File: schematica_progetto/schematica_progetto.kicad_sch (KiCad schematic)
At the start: 7 parts

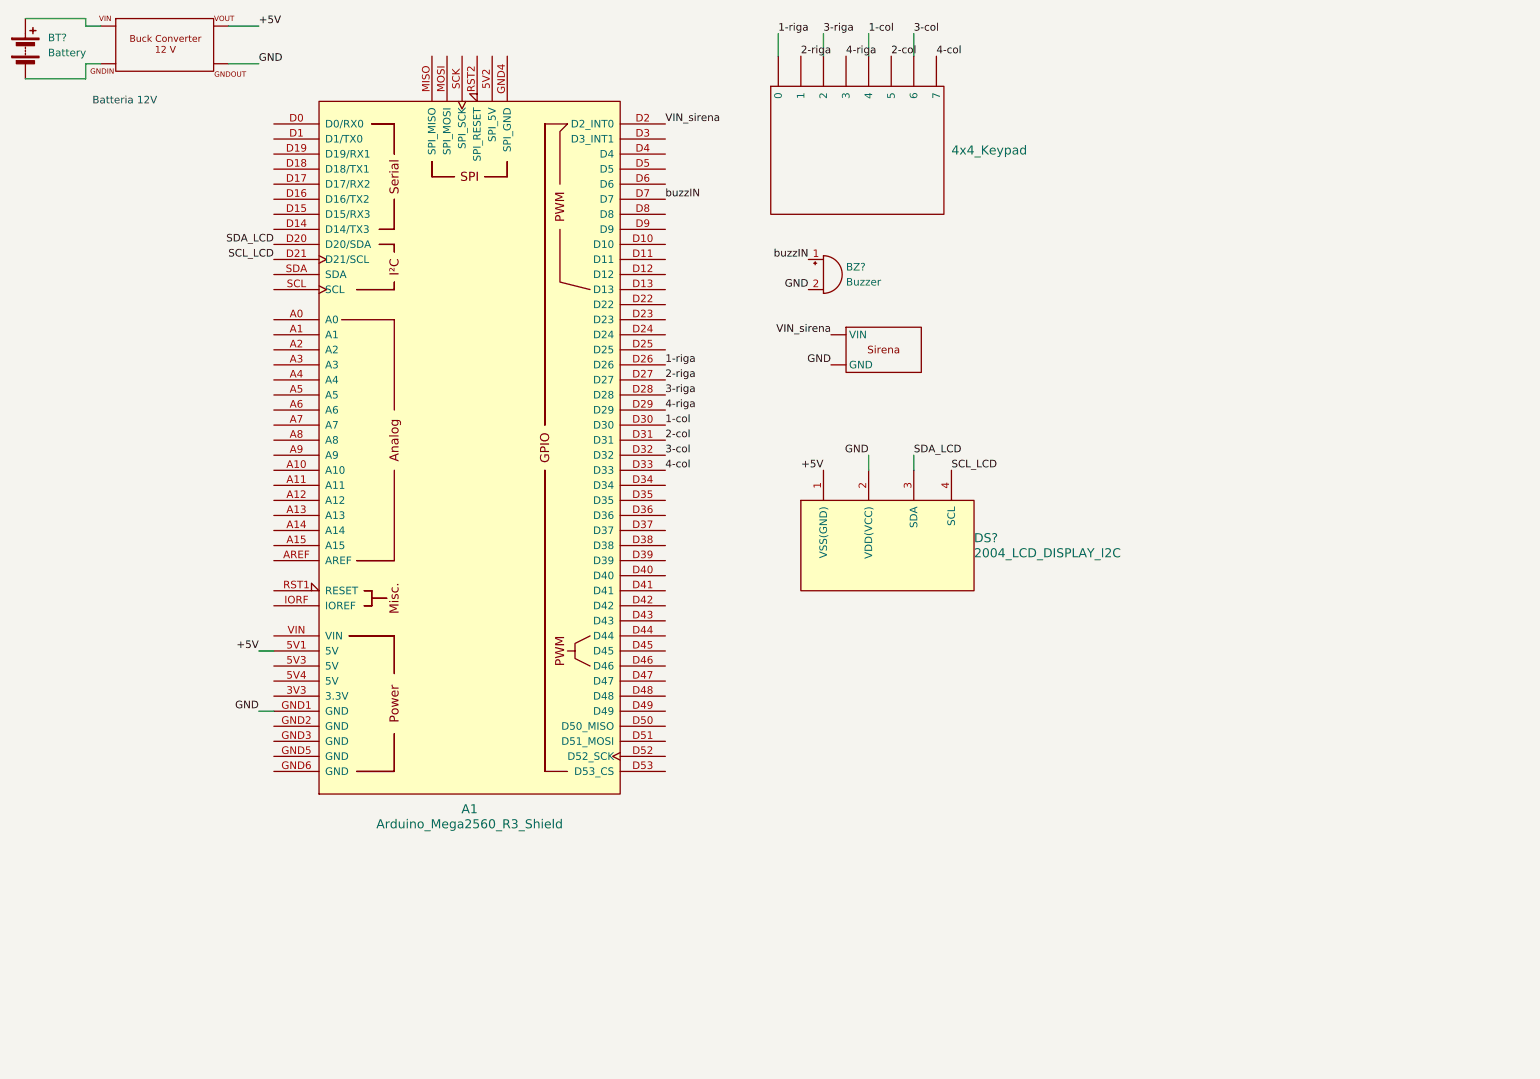
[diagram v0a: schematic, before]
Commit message: Inserito nella schematica sistema di controllo dei LED dei pulsanti. Terminata la schematica
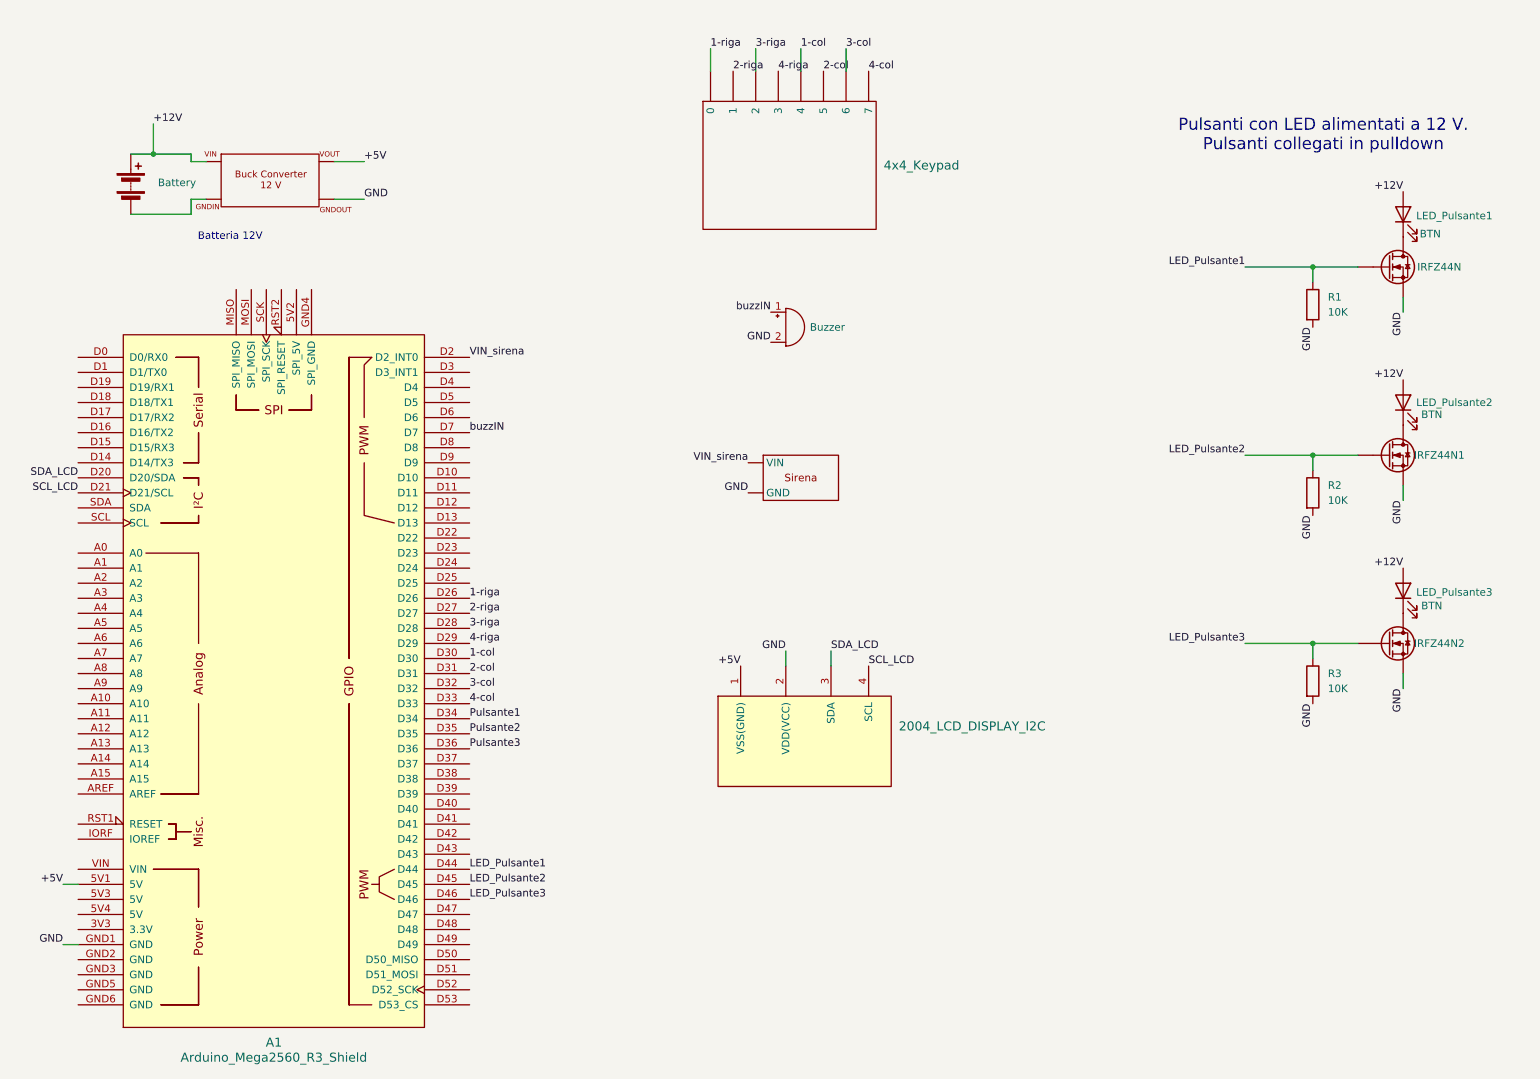
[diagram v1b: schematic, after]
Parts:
- added IRFZ44N, IRFZ44N1, IRFZ44N2: (no value), symbol Device:Q_NMOS
- added LED_Pulsante1, LED_Pulsante2, LED_Pulsante3: BTN, symbol Device:LED
- added R1, R2, R3: 10K, symbol Device:R
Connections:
- net GND: now also IRFZ44N.S, IRFZ44N1.S, IRFZ44N2.S, R1.2, R2.2, R3.2
- net +12V: now reaches BT?.1 (+), U?.
- net +12V: now also LED_Pulsante1.2 (A), LED_Pulsante2.2 (A), LED_Pulsante3.2 (A)
- net Pulsante1: now reaches A1.D34
- net Pulsante2: now reaches A1.D35
- net Pulsante3: now reaches A1.D36
- net LED_Pulsante1: now reaches A1.D44
- net LED_Pulsante1: now also IRFZ44N.G, R1.1
- net LED_Pulsante2: now reaches A1.D45
- net LED_Pulsante2: now also IRFZ44N1.G, R2.1
- net LED_Pulsante3: now reaches A1.D46
- net LED_Pulsante3: now also IRFZ44N2.G, R3.1
- new net: IRFZ44N1.D, LED_Pulsante2.1 (K)
- new net: IRFZ44N2.D, LED_Pulsante3.1 (K)
- new net: IRFZ44N.D, LED_Pulsante1.1 (K)
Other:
- note added: "Pulsanti con LED alimentati a 12 V. Pulsanti collegati in pulldown"
- moved on the sheet: A1

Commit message: Aggiunto sirena e accellerometro
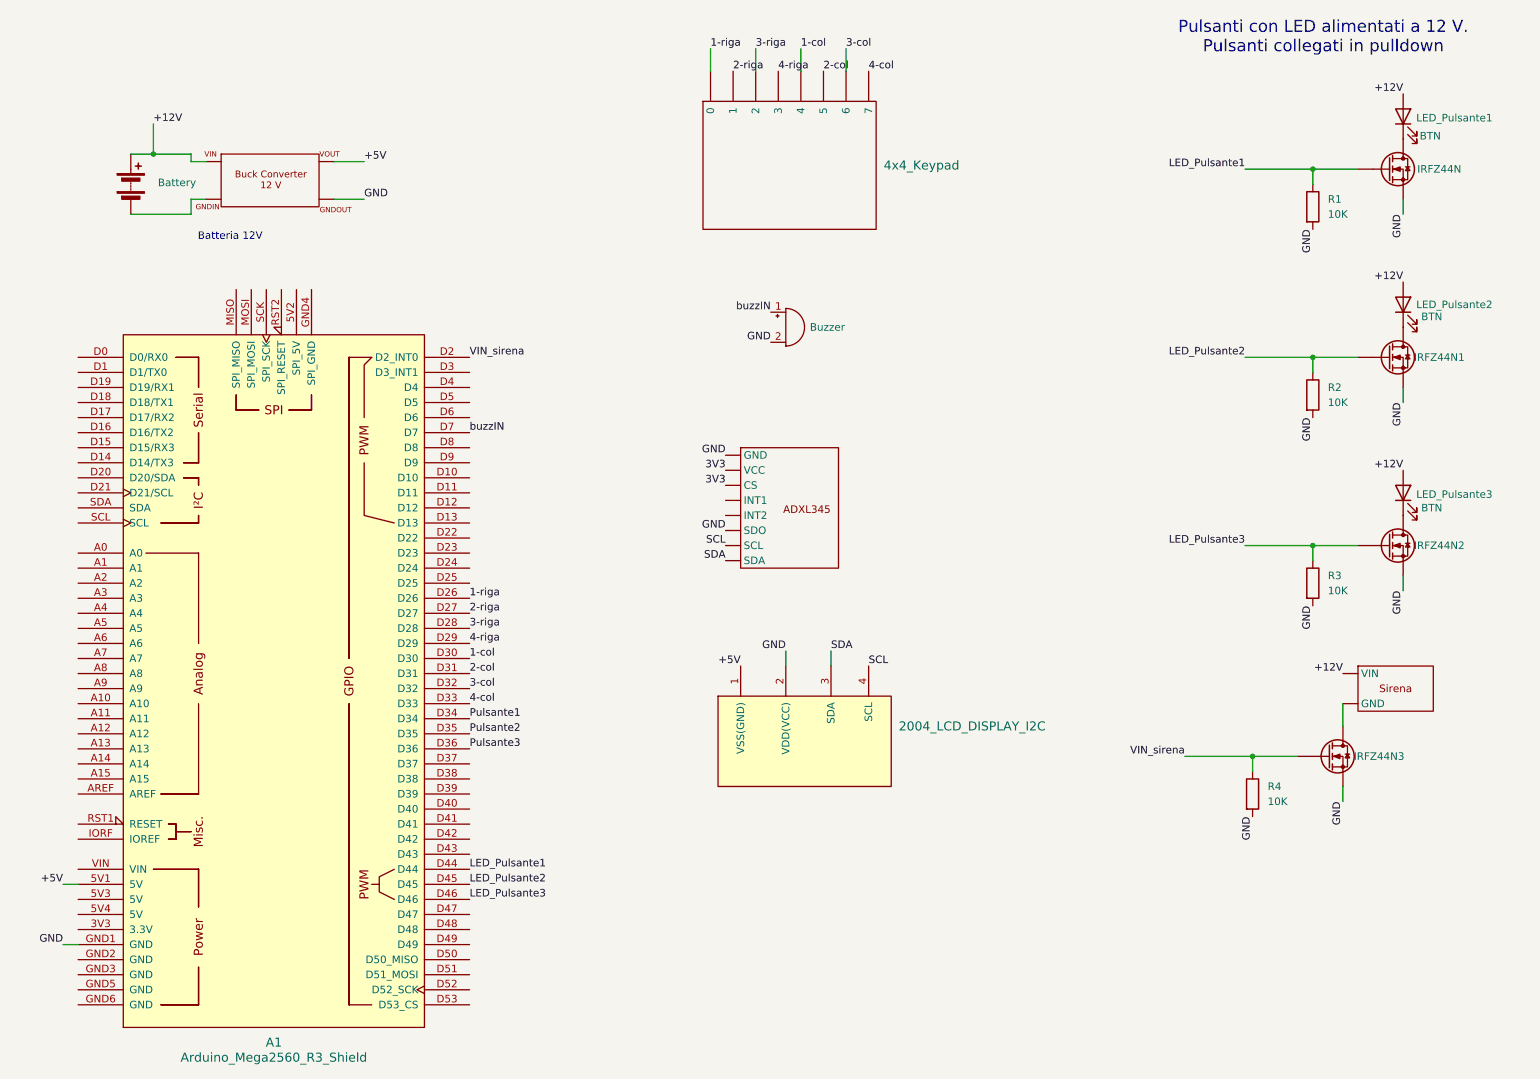
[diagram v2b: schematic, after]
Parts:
- removed U?: (no value), symbol simboli_personali:sirena
- added IRFZ44N3: (no value), symbol Device:Q_NMOS
- added R4: 10K, symbol Device:R
- added U1: (no value), symbol simboli_personali:ADXL345
- added U2: (no value), symbol simboli_personali:sirena
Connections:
- net +12V: now also U2. (GND)
- net GND: now also IRFZ44N3.S, R4.2, U1. (SDA)
- net VIN_sirena: now also IRFZ44N3.G, R4.1
- net SCL_LCD: no longer names the net of A1.D21 (D21/SCL)
- net SCL_LCD: no longer DS?.4 (SCL)
- net SDA_LCD: no longer names the net of A1.D20 (D20/SDA)
- net SDA_LCD: no longer DS?.3 (SDA)
- new net: IRFZ44N3.D, U2. (GND)
- new net 3V3: U1. (SDA)
- new net SCL: DS?.4 (SCL), U1. (SDA)
- new net SDA: DS?.3 (SDA), U1. (SDA)
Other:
- moved on the sheet: IRFZ44N, IRFZ44N1, IRFZ44N2, LED_Pulsante1, LED_Pulsante2, LED_Pulsante3, R1, R2, R3
